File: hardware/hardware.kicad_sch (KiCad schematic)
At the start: 25 parts, among them J1 USB_B_Micro, J2 Conn_Coaxial, Q1 BSS138, Q2 BSS138, U1 ESP32-WROOM-32, U2 AMS1117-3.3, U4 CH340C, U5 RFM95W-868S2

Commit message: add nunchuck footprint
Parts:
- U3: footprint wii:nunchuck -> nunchcuk:nunchuck
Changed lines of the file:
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@@
 			)
 		)
-		(property "Footprint" "wii:nunchuck"
+		(property "Footprint" "nunchcuk:nunchuck"
 			(at 128.27 80.01 0)
 			(effects

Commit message: lora wiring + pcb wiring
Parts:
- added J3: Conn_01x04, Connector_PinHeader_2.54mm:PinHeader_1x04_P2.54mm_Vertical, symbol Connector_Generic:Conn_01x04
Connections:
- net +3V3: now also J3.4 (Pin_4)
- net DIO0: now also U1.27 (IO16)
- net DIO1: now also U1.28 (IO17)
- net DIO2: now also U1.30 (IO18)
- net GND: now also J3.3 (Pin_3)
- net MISO: now also U1.14 (IO12)
- net MOSI: now also U1.16 (IO13)
- net SCL: now also J3.1 (Pin_1)
- net SCLK: now also U1.13 (IO14)
- net SDA: now also J3.2 (Pin_2)
- net SS: now also U1.23 (IO15)
- net at U1.11 (IO26): now also R5.1
- net at U1.12 (IO27): now also R6.1
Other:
- moved on the sheet: D1, D2, R2, R3, R5, R6

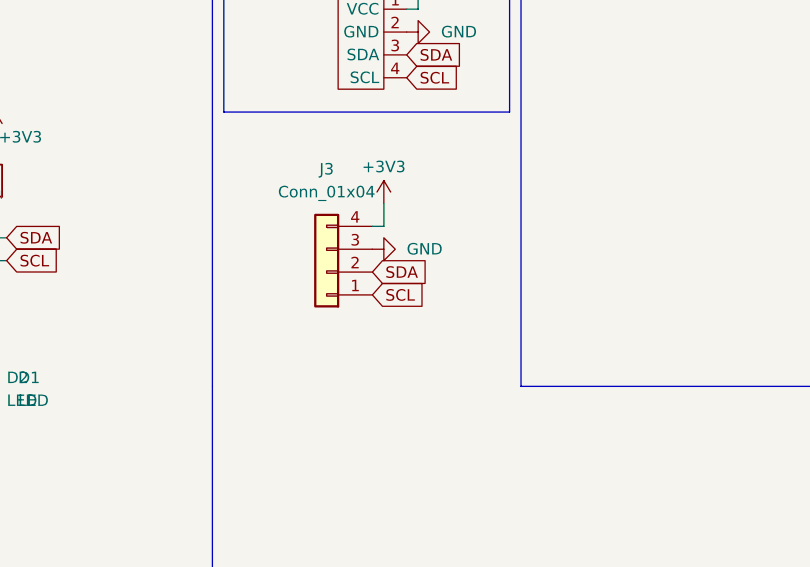
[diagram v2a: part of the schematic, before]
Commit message: invert i2c screen wiring
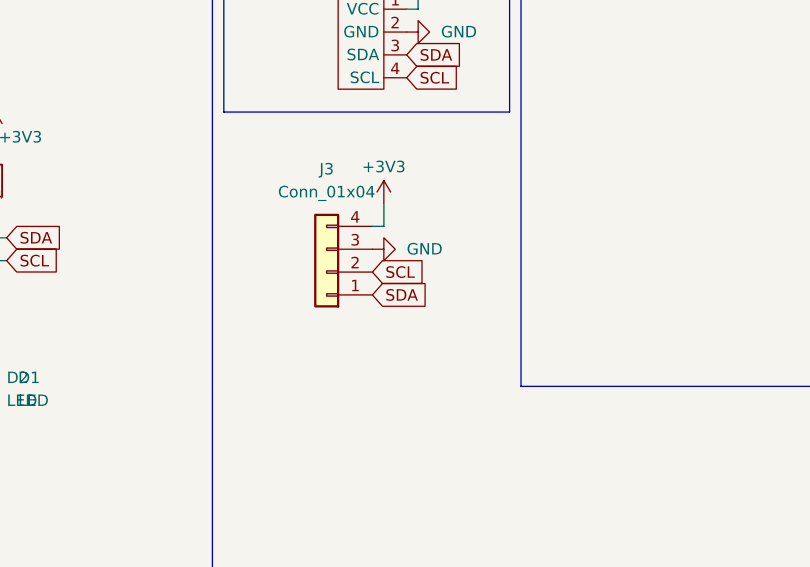
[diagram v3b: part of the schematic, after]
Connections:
- net SCL: now also J3.2 (Pin_2); no longer J3.1 (Pin_1)
- net SDA: now also J3.1 (Pin_1); no longer J3.2 (Pin_2)

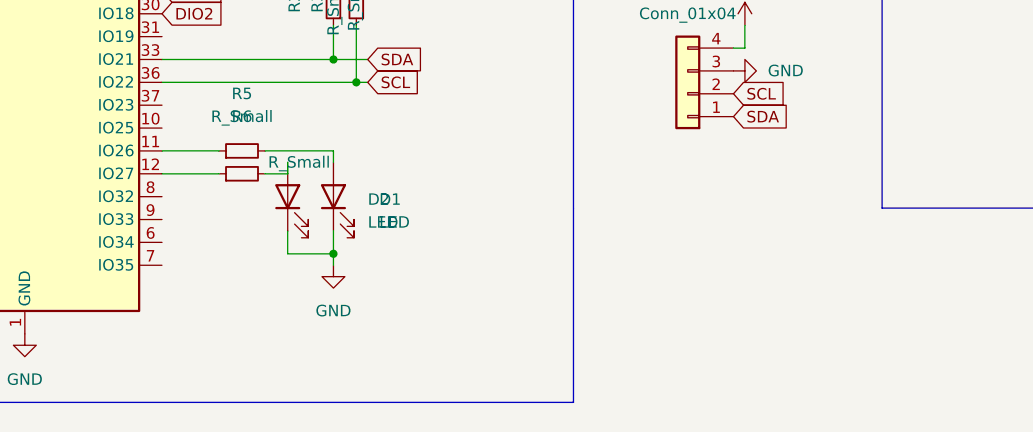
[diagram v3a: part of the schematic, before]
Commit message: add second nunchuck connector and pcb wiring
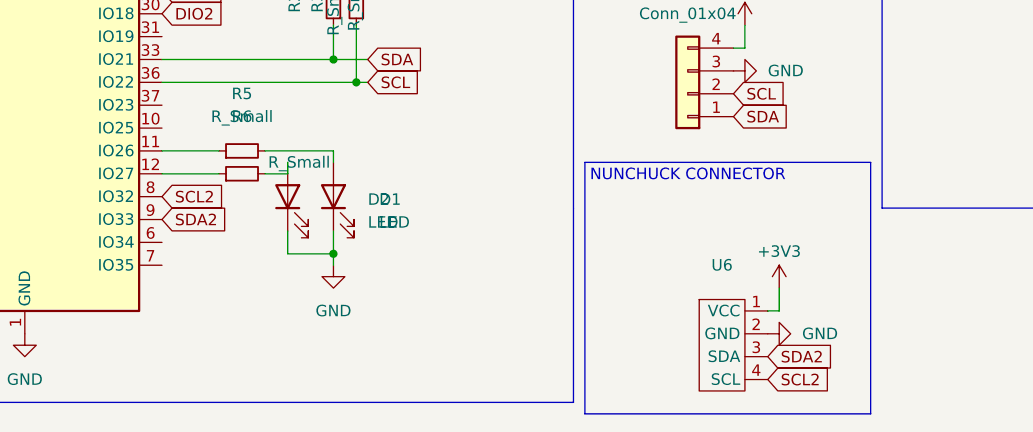
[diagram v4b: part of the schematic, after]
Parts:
- added U6: ~, nunchcuk:nunchuck, symbol Nunchuck:Nunchuck
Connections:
- net +3V3: now also U6.1 (VCC)
- net GND: now also U6.2 (GND)
- net SCL2: now reaches U1.8 (IO32)
- net SCL2: now also U6.4 (SCL)
- net SDA2: now reaches U1.9 (IO33)
- net SDA2: now also U6.3 (SDA)

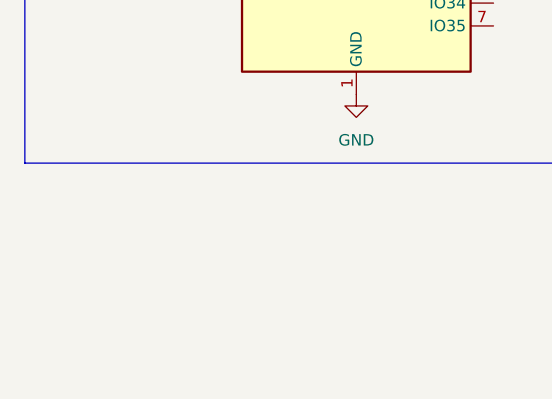
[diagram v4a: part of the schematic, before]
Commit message: add ftdi pin and wiring to esp
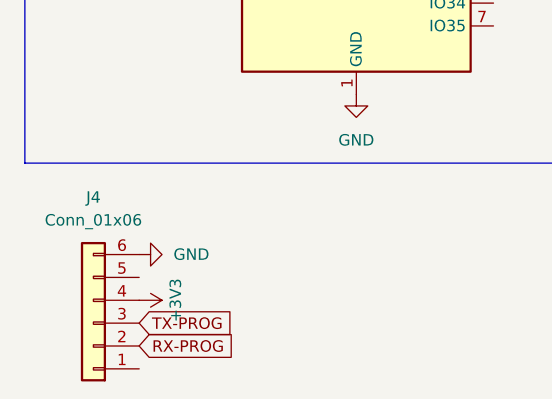
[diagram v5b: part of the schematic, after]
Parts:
- added J4: Conn_01x06, Connector_PinHeader_2.54mm:PinHeader_1x06_P2.54mm_Vertical, symbol Connector_Generic:Conn_01x06
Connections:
- net +3V3: now also J4.4 (Pin_4)
- net GND: now also J4.6 (Pin_6)
- net RX-PROG: now also J4.2 (Pin_2)
- net TX-PROG: now also J4.3 (Pin_3)

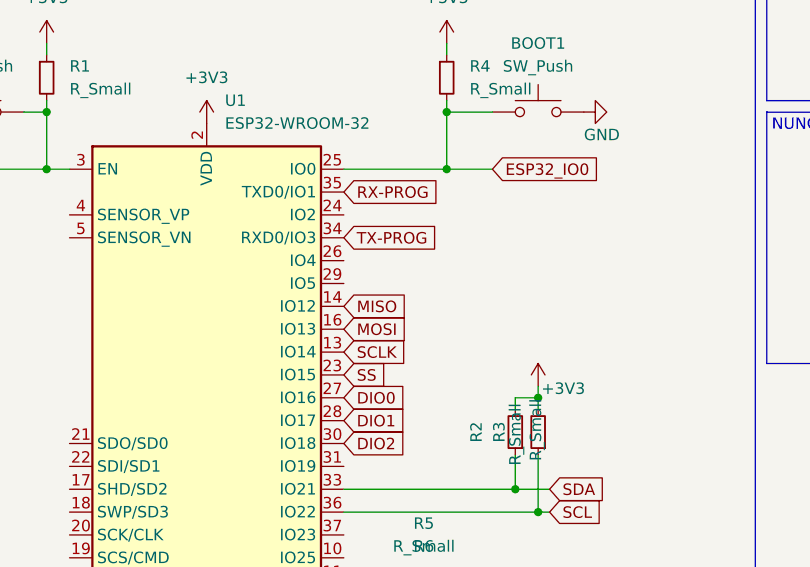
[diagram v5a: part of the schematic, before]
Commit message: fix i2c wiring and lora rst
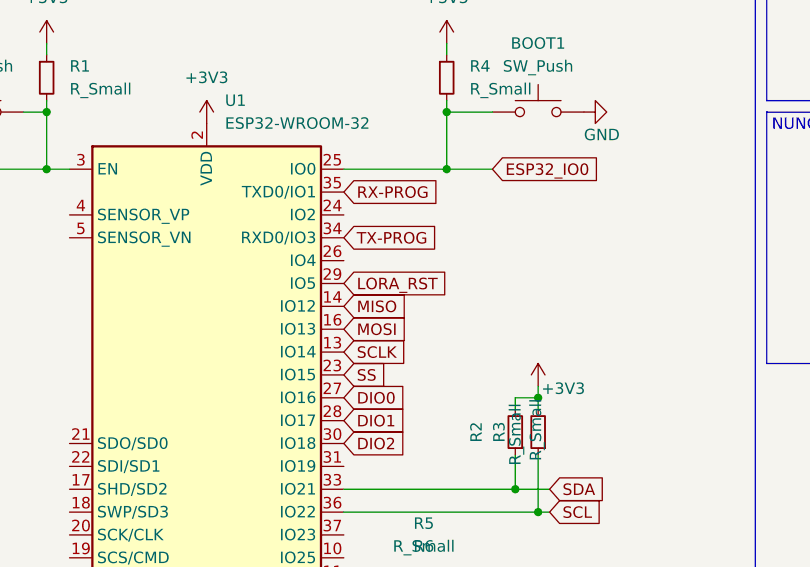
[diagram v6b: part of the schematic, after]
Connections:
- net LORA_RST: now also U1.29 (IO5)
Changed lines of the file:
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@@
+		)
+	)
+	(global_label "LORA_RST"
+		(shape input)
+		(at 66.04 83.82 0)
+		(fields_autoplaced yes)
+		(effects
+			(font
+				(size 1.27 1.27)
+			)
+			(justify left)
+		)
+		(property "Intersheetrefs" "${INTERSHEET_REFS}"
+			(at 78.1571 83.82 0)
+			(effects
+				(font
+					(size 1.27 1.27)
+				)
+				(justify left)
+				(hide yes)
+			)
 		)
 	)
